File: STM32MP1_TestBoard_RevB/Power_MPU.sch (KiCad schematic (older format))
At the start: 30 parts, among them U1 STM32MP157xAB

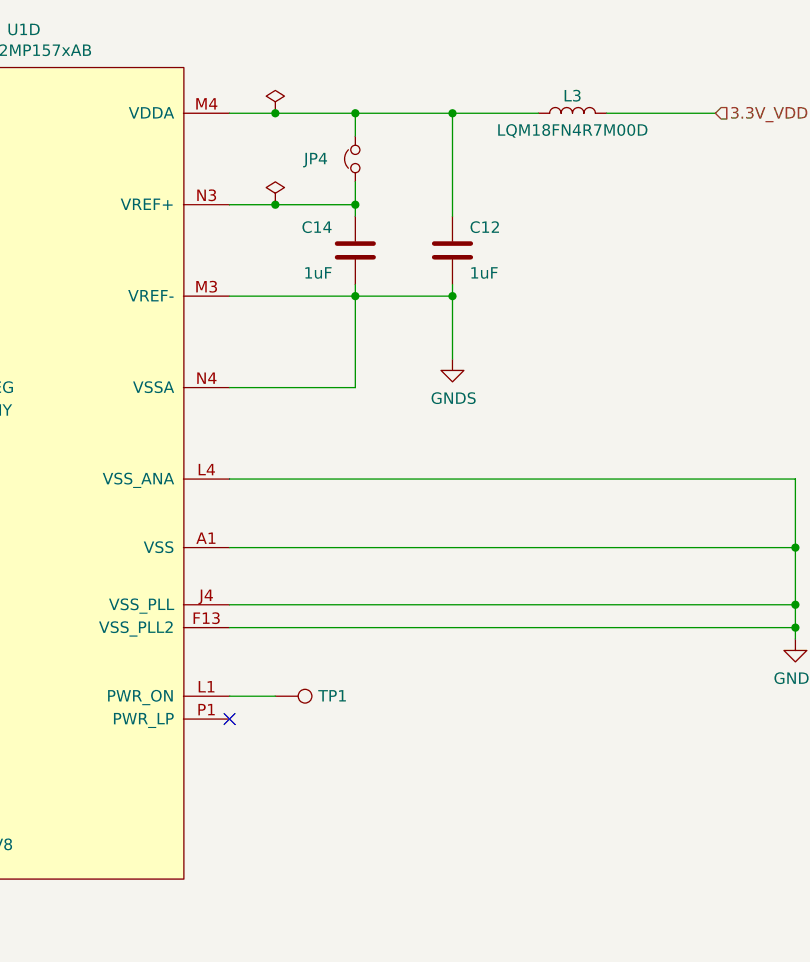
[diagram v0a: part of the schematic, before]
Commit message: Updated design
- Added Crystal/Oscillators
- Replaced both SDMMC with single SDMMC w/ detect pin
- Added USB Type C for VIN
- Moved SWD pins
- Tidied up silk screen for pin headers J1, J2, J3, J4
- Moved DSI socket
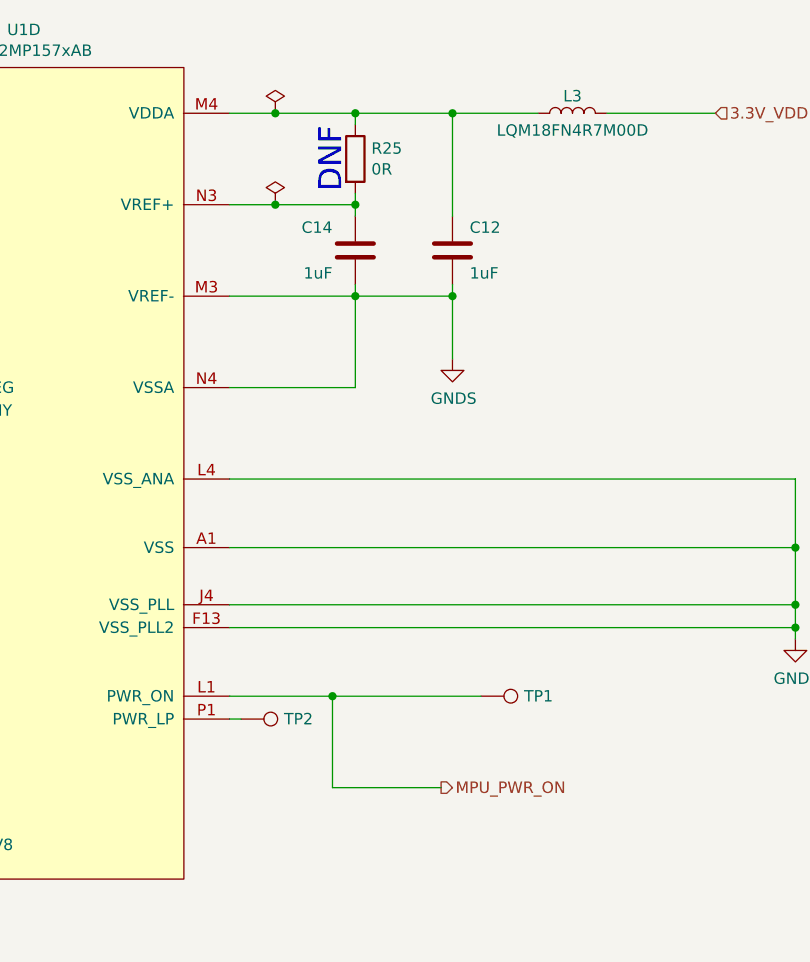
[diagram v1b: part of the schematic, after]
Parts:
- removed JP4: Jumper_NC_Small, Jumper:SolderJumper-2_P1.3mm_Bridged_Pad1.0x1.5mm, symbol Device:Jumper_NC_Small
- added R25: 0R, Capacitor_SMD:C_0402_1005Metric_Pad0.74x0.62mm_HandSolder, symbol Device:R
- added TP2: TestPoint, TestPoint:TestPoint_Pad_D1.0mm, symbol Connector:TestPoint
- C12, C14, C17, C18, C19, C20, C21, C22, C23, C24, C25, C26, C27, C28, C29, C30, C31, C32, C33, C34, C35, C68, C70: LCSC (none) -> C52923
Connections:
- net MPU_PWR_ON: now reaches TP1.1, U1.L1 (PWR_ON)
- net at C12.2, L3.2, U1.M4 (VDDA): now also R25.1
- net at C14.2, U1.N3 (VREF+): now also R25.2
- net at U1.P1 (PWR_LP): now also TP2.1
- no-connect marks 1 -> 0
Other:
- note added: "DNF"
- moved on the sheet: TP1
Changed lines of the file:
@@
 $Descr A3 16535 11693
 encoding utf-8
-Sheet 2 10
+Sheet 2 9
 Title ""
 Date ""
@@
 F 4 "Taiyo Yuden" H 6500 5725 50  0001 C CNN "Mfr"
 F 5 "LMK105BJ105KV-F" H 6500 5725 50  0001 C CNN "PartNo"
+F 6 "C52923" H 6500 5725 50  0001 C CNN "LCSC"
 	1    6500 5725
 	1    0    0    -1
@@
 F 4 "Taiyo Yuden" H 3800 8450 50  0001 C CNN "Mfr"
 F 5 "LMK105BJ105KV-F" H 3800 8450 50  0001 C CNN "PartNo"
+F 6 "C52923" H 3800 8450 50  0001 C CNN "LCSC"
 	1    3800 8450
 	1    0    0    -1
@@
 F 4 "Taiyo Yuden" H 4200 8450 50  0001 C CNN "Mfr"
 F 5 "LMK105BJ105KV-F" H 4200 8450 50  0001 C CNN "PartNo"
+F 6 "C52923" H 4200 8450 50  0001 C CNN "LCSC"
 	1    4200 8450
 	1    0    0    -1
@@
 F 4 "Taiyo Yuden" H 4625 8450 50  0001 C CNN "Mfr"
 F 5 "LMK105BJ105KV-F" H 4625 8450 50  0001 C CNN "PartNo"
+F 6 "C52923" H 4625 8450 50  0001 C CNN "LCSC"
 	1    4625 8450
 	1    0    0    -1
@@
 F 4 "Taiyo Yuden" H 5025 8450 50  0001 C CNN "Mfr"
 F 5 "LMK105BJ105KV-F" H 5025 8450 50  0001 C CNN "PartNo"
+F 6 "C52923" H 5025 8450 50  0001 C CNN "LCSC"
 	1    5025 8450
 	1    0    0    -1
@@
 F 4 "Taiyo Yuden" H 5425 8450 50  0001 C CNN "Mfr"
 F 5 "LMK105BJ105KV-F" H 5425 8450 50  0001 C CNN "PartNo"
+F 6 "C52923" H 5425 8450 50  0001 C CNN "LCSC"
 	1    5425 8450
 	1    0    0    -1
@@
 F 4 "Taiyo Yuden" H 5825 8450 50  0001 C CNN "Mfr"
 F 5 "LMK105BJ105KV-F" H 5825 8450 50  0001 C CNN "PartNo"
+F 6 "C52923" H 5825 8450 50  0001 C CNN "LCSC"
 	1    5825 8450
 	1    0    0    -1
@@
 F 4 "Taiyo Yuden" H 6225 8450 50  0001 C CNN "Mfr"
 F 5 "LMK105BJ105KV-F" H 6225 8450 50  0001 C CNN "PartNo"
+F 6 "C52923" H 6225 8450 50  0001 C CNN "LCSC"
 	1    6225 8450
 	1    0    0    -1
@@
 F 4 "Taiyo Yuden" H 6650 8450 50  0001 C CNN "Mfr"
 F 5 "LMK105BJ105KV-F" H 6650 8450 50  0001 C CNN "PartNo"
+F 6 "C52923" H 6650 8450 50  0001 C CNN "LCSC"
 	1    6650 8450
 	1    0    0    -1
@@
 F 4 "Taiyo Yuden" H 8500 8425 50  0001 C CNN "Mfr"
 F 5 "LMK105BJ105KV-F" H 8500 8425 50  0001 C CNN "PartNo"
+F 6 "C52923" H 8500 8425 50  0001 C CNN "LCSC"
 	1    8500 8425
 	1    0    0    -1
@@
 F 4 "Taiyo Yuden" H 8900 8425 50  0001 C CNN "Mfr"
 F 5 "LMK105BJ105KV-F" H 8900 8425 50  0001 C CNN "PartNo"
+F 6 "C52923" H 8900 8425 50  0001 C CNN "LCSC"
 	1    8900 8425
 	1    0    0    -1
@@
 F 4 "Taiyo Yuden" H 9325 8425 50  0001 C CNN "Mfr"
 F 5 "LMK105BJ105KV-F" H 9325 8425 50  0001 C CNN "PartNo"
+F 6 "C52923" H 9325 8425 50  0001 C CNN "LCSC"
 	1    9325 8425
 	1    0    0    -1
@@
 F 4 "Taiyo Yuden" H 9725 8425 50  0001 C CNN "Mfr"
 F 5 "LMK105BJ105KV-F" H 9725 8425 50  0001 C CNN "PartNo"
+F 6 "C52923" H 9725 8425 50  0001 C CNN "LCSC"
 	1    9725 8425
 	1    0    0    -1
@@
 F 4 "Taiyo Yuden" H 10125 8425 50  0001 C CNN "Mfr"
 F 5 "LMK105BJ105KV-F" H 10125 8425 50  0001 C CNN "PartNo"
+F 6 "C52923" H 10125 8425 50  0001 C CNN "LCSC"
 	1    10125 8425
 	1    0    0    -1
@@
 F 4 "Taiyo Yuden" H 10525 8425 50  0001 C CNN "Mfr"
 F 5 "LMK105BJ105KV-F" H 10525 8425 50  0001 C CNN "PartNo"
+F 6 "C52923" H 10525 8425 50  0001 C CNN "LCSC"
 	1    10525 8425
 	1    0    0    -1
@@
 F 4 "Taiyo Yuden" H 12275 8425 50  0001 C CNN "Mfr"
 F 5 "LMK105BJ105KV-F" H 12275 8425 50  0001 C CNN "PartNo"
+F 6 "C52923" H 12275 8425 50  0001 C CNN "LCSC"
 	1    12275 8425
 	1    0    0    -1
@@
 F 4 "Taiyo Yuden" H 12675 8425 50  0001 C CNN "Mfr"
 F 5 "LMK105BJ105KV-F" H 12675 8425 50  0001 C CNN "PartNo"
+F 6 "C52923" H 12675 8425 50  0001 C CNN "LCSC"
 	1    12675 8425
 	1    0    0    -1
@@
 F 4 "Taiyo Yuden" H 13100 8425 50  0001 C CNN "Mfr"
 F 5 "LMK105BJ105KV-F" H 13100 8425 50  0001 C CNN "PartNo"
+F 6 "C52923" H 13100 8425 50  0001 C CNN "LCSC"
 	1    13100 8425
 	1    0    0    -1
@@
 F 4 "Taiyo Yuden" H 13500 8425 50  0001 C CNN "Mfr"
 F 5 "LMK105BJ105KV-F" H 13500 8425 50  0001 C CNN "PartNo"
+F 6 "C52923" H 13500 8425 50  0001 C CNN "LCSC"
 	1    13500 8425
 	1    0    0    -1
@@
 F 4 "~" H 10575 2875 50  0001 C CNN "Mfr"
 F 5 "~" H 10575 2875 50  0001 C CNN "PartNo"
+F 6 "~" H 10575 2875 50  0001 C CNN "LCSC"
 	1    10575 2875
 	0    1    -1   0
@@
 F 4 "Taiyo Yuden" H 9625 3475 50  0001 C CNN "Mfr"
 F 5 "LMK105BJ105KV-F" H 9625 3475 50  0001 C CNN "PartNo"
+F 6 "C52923" H 9625 3475 50  0001 C CNN "LCSC"
 	1    9625 3475
 	-1   0    0    1
@@
 F 4 "Taiyo Yuden" H 10050 3475 50  0001 C CNN "Mfr"
 F 5 "LMK105BJ105KV-F" H 10050 3475 50  0001 C CNN "PartNo"
+F 6 "C52923" H 10050 3475 50  0001 C CNN "LCSC"
 	1    10050 3475
 	1    0    0    1
@@
 Wire Wire Line
 	9075 2875 9275 2875
-$Comp
-L Device:Jumper_NC_Small JP4
-U 1 1 5FDCA779
-P 9625 3075
-F 0 "JP4" V 9625 3300 50  0000 R CNN
-F 1 "Jumper_NC_Small" V 9670 3149 50  0001 L CNN
-F 2 "Jumper:SolderJumper-2_P1.3mm_Bridged_Pad1.0x1.5mm" H 9625 3075 50  0001 C CNN
-F 3 "~" H 9625 3075 50  0001 C CNN
-F 4 "~" H 9625 3075 50  0001 C CNN "Mfr"
-F 5 "~" H 9625 3075 50  0001 C CNN "PartNo"
-	1    9625 3075
-	0    -1   -1   0
-$EndComp
-Wire Wire Line
-	9625 2975 9625 2875
+Wire Wire Line
+	9625 2925 9625 2875
 Connection ~ 9625 2875
 Wire Wire Line
 	9625 2875 10050 2875
 Wire Wire Line
-	9625 3175 9625 3275
+	9625 3225 9625 3275
 Connection ~ 9625 3275
 Wire Wire Line
@@
 F 4 "Taiyo Yuden" H 5525 4375 50  0001 C CNN "Mfr"
 F 5 "LMK105BJ105KV-F" H 5525 4375 50  0001 C CNN "PartNo"
+F 6 "~" H 5525 4375 50  0001 C CNN "LCSC"
 	1    5525 4375
 	-1   0    0    1
@@
 F 4 "Taiyo Yuden" H 5525 4775 50  0001 C CNN "Mfr"
 F 5 "LMK105BJ105KV-F" H 5525 4775 50  0001 C CNN "PartNo"
+F 6 "C52923" H 5525 4775 50  0001 C CNN "LCSC"
 	1    5525 4775
 	-1   0    0    1
@@
 F 4 "Taiyo Yuden" H 6750 5725 50  0001 C CNN "Mfr"
 F 5 "LMK105BJ105KV-F" H 6750 5725 50  0001 C CNN "PartNo"
+F 6 "C52923" H 6750 5725 50  0001 C CNN "LCSC"
 	1    6750 5725
 	-1   0    0    -1
@@
 F 4 "Taiyo Yuden" H 5175 5700 50  0001 C CNN "Mfr"
 F 5 "LMK105BJ105KV-F" H 5175 5700 50  0001 C CNN "PartNo"
+F 6 "~" H 5175 5700 50  0001 C CNN "LCSC"
 	1    5175 5700
 	1    0    0    -1
@@
 F 4 "Taiyo Yuden" H 5525 5700 50  0001 C CNN "Mfr"
 F 5 "LMK105BJ105KV-F" H 5525 5700 50  0001 C CNN "PartNo"
+F 6 "~" H 5525 5700 50  0001 C CNN "LCSC"
 	1    5525 5700
 	-1   0    0    1
@@
 	6100 4075 5525 4075
 Connection ~ 5175 5125
-NoConn ~ 9075 5525
 Wire Wire Line
 	7275 3525 6900 3525
@@
 F 4 "~" H 8175 4425 50  0001 C CNN "Mfr"
 F 5 "~" H 8175 4425 50  0001 C CNN "PartNo"
+F 6 "~" H 8175 4425 50  0001 C CNN "LCSC"
 	4    8175 4425
 	1    0    0    -1
@@
 L Connector:TestPoint TP1
 U 1 1 5FCFAF5B
-P 9275 5425
-F 0 "TP1" V 9275 5613 50  0000 L CNN
-F 1 "TestPoint" V 9320 5613 50  0001 L CNN
-F 2 "TestPoint:TestPoint_Pad_D1.0mm" H 9475 5425 50  0001 C CNN
-F 3 "~" H 9475 5425 50  0001 C CNN
-F 4 "~" H 9275 5425 50  0001 C CNN "Mfr"
-F 5 "~" H 9275 5425 50  0001 C CNN "PartNo"
-	1    9275 5425
+P 10175 5425
+F 0 "TP1" V 10175 5613 50  0000 L CNN
+F 1 "TestPoint" V 10220 5613 50  0001 L CNN
+F 2 "TestPoint:TestPoint_Pad_D1.0mm" H 10375 5425 50  0001 C CNN
+F 3 "~" H 10375 5425 50  0001 C CNN
+F 4 "~" H 10175 5425 50  0001 C CNN "Mfr"
+F 5 "~" H 10175 5425 50  0001 C CNN "PartNo"
+F 6 "~" H 10175 5425 50  0001 C CNN "LCSC"
+	1    10175 5425
 	0    1    1    0
 $EndComp
 Wire Wire Line
-	9075 5425 9275 5425
+	9075 5425 9525 5425
 Text HLabel 4775 5125 0    50   Output ~ 0
 1V8_DETECT
+Wire Wire Line
+	9525 5425 9525 5825
+Wire Wire Line
+	9525 5825 10000 5825
+Connection ~ 9525 5425
+Wire Wire Line
+	9525 5425 10175 5425
+Text HLabel 10000 5825 2    50   Output ~ 0
+MPU_PWR_ON
+$Comp
+L Device:R R25
+U 1 1 60CAAF0A
+P 9625 3075
+F 0 "R25" H 9695 3121 50  0000 L CNN
+F 1 "0R" H 9695 3030 50  0000 L CNN
+F 2 "Capacitor_SMD:C_0402_1005Metric_Pad0.74x0.62mm_HandSolder" V 9555 3075 50  0001 C CNN
+F 3 "~" H 9625 3075 50  0001 C CNN
+	1    9625 3075
+	1    0    0    -1
+$EndComp
+Text Notes 9575 3225 1    100  ~ 0
+DNF
+$Comp
+L Connector:TestPoint TP2
+U 1 1 611C0EB3
+P 9125 5525
+F 0 "TP2" V 9125 5713 50  0000 L CNN
+F 1 "TestPoint" V 9170 5713 50  0001 L CNN
+F 2 "TestPoint:TestPoint_Pad_D1.0mm" H 9325 5525 50  0001 C CNN
+F 3 "~" H 9325 5525 50  0001 C CNN
+F 4 "~" H 9125 5525 50  0001 C CNN "Mfr"
+F 5 "~" H 9125 5525 50  0001 C CNN "PartNo"
+F 6 "~" H 9125 5525 50  0001 C CNN "LCSC"
+	1    9125 5525
+	0    1    1    0
+$EndComp
+Wire Wire Line
+	9125 5525 9075 5525
 $EndSCHEMATC

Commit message: completed revb layout
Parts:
- added C38: 100nF, Capacitor_SMD:C_0402_1005Metric_Pad0.74x0.62mm_HandSolder, symbol Device:C
- added J12: Conn_01x02, Connector_Molex:Molex_KK-254_AE-6410-02A_1x02_P2.54mm_Vertical, symbol Connector_Generic:Conn_01x02
- L3: Mouser (none) -> 81-LQM18FN4R7M00D
- R25: LCSC (none) -> C25087
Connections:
- net 3.3V_VDD: no longer U1.H3 (VBAT)
- net GNDS: now also C38.1, J12.2 (Pin_2)
- new net VBAT: C38.2, J12.1 (Pin_1), U1.H3 (VBAT)
